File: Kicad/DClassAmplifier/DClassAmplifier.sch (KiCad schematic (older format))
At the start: 16 parts

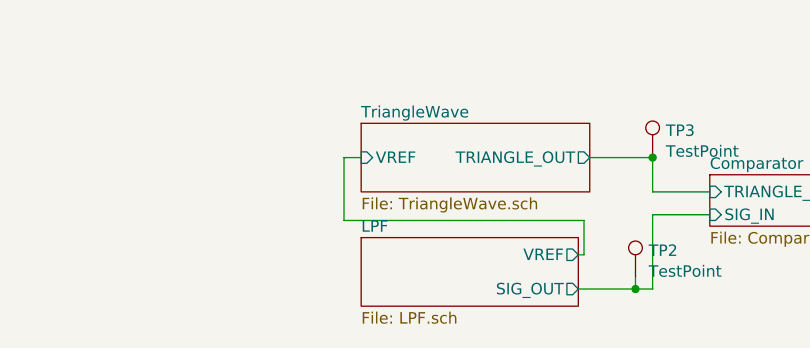
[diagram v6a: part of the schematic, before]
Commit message: Added input to global schematic
Changed the sig_in net label in the LPF sheet to a hierarchical net label of the same name
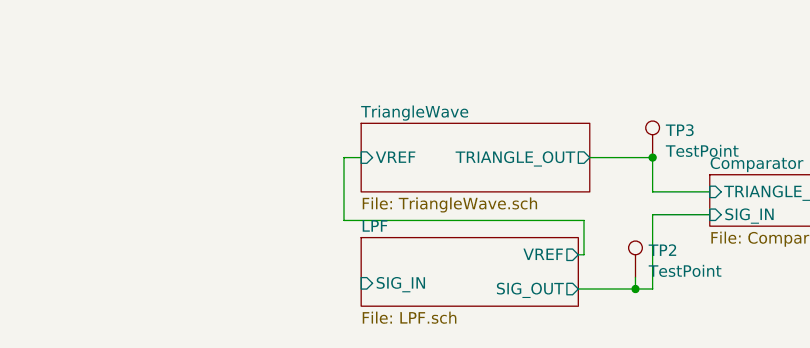
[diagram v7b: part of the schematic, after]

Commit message: Combined Board
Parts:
- removed TP5: TestPoint, TestPoint:TestPoint_Pad_D2.0mm, symbol Connector:TestPoint
- added J1, J3, J4, J5: Conn_01x02, TerminalBlock:TerminalBlock_bornier-2_P5.08mm, symbol Connector_Generic:Conn_01x02
- added J2: Conn_01x03, TerminalBlock:TerminalBlock_bornier-3_P5.08mm, symbol Connector_Generic:Conn_01x03
- added TP2: TestPoint, TestPoint:TestPoint_THTPad_D1.5mm_Drill0.7mm, symbol Connector:TestPoint
- TP1: footprint TestPoint:TestPoint_Pad_D2.0mm -> TestPoint:TestPoint_THTPad_D1.5mm_Drill0.7mm
- TP3: renamed from TP4; footprint TestPoint:TestPoint_Pad_D2.0mm -> TestPoint:TestPoint_THTPad_D1.5mm_Drill0.7mm
- TP4: renamed from TP3; footprint TestPoint:TestPoint_Pad_D2.0mm -> TestPoint:TestPoint_THTPad_D1.5mm_Drill0.7mm
- TP5: renamed from TP6; footprint TestPoint:TestPoint_Pad_D2.0mm -> TestPoint:TestPoint_THTPad_D1.5mm_Drill0.7mm
- TP6: renamed from TP8; footprint TestPoint:TestPoint_Pad_D2.0mm -> TestPoint:TestPoint_THTPad_D1.5mm_Drill0.7mm
- TP7: renamed from TP9; footprint TestPoint:TestPoint_Pad_D2.0mm -> TestPoint:TestPoint_THTPad_D1.5mm_Drill0.7mm
- TP8: renamed from TP7; footprint TestPoint:TestPoint_Pad_D2.0mm -> TestPoint:TestPoint_THTPad_D1.5mm_Drill0.7mm
- TP9: renamed from TP2; footprint TestPoint:TestPoint_Pad_D2.0mm -> TestPoint:TestPoint_THTPad_D1.5mm_Drill0.7mm
- renumbered C15 to C2, H3 to H2, H2 to H3
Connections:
- net Comparator/INV_PWM_OUT: now also J2.2 (Pin_2), TP2.1
- net Comparator/PWM_OUT: now also J2.1 (Pin_1)
- net GND: now also J2.3 (Pin_3), J3.2 (Pin_2), J5.2 (Pin_2)
- net GNDPWR: now also J1.2 (Pin_2)
- net OutputFilter/SPEAKER+: now also J4.2 (Pin_2)
- net OutputFilter/SPEAKER-: now also J4.1 (Pin_1)
- net VDD: now also J1.1 (Pin_1)
- new net SIG_IN: J5.1 (Pin_1)
- new net VCC: J3.1 (Pin_1)
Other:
- moved on the sheet: TP3
